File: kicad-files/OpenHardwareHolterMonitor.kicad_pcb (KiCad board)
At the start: 6 copper layers, 131 x 80 mm, 155 parts, among them CON1 Micro_SD_Card, J1 Conn_02x06_Odd_Even, J10 Conn_01x01, J11 Conn_01x01, J12 USB_OTG, J13 USB_C_Receptacle, J2 Conn_01x01, J3 Conn_01x01, J4 Conn_01x01, J5 Conn_01x01, J6 Conn_01x01, J7 Conn_01x01, J8 Conn_01x01, J9 Conn_01x01, P1 Custom_FTDI, Q1 S8050, Q10 Q_PMOS_DGS, Q2 S8050, Q3 Q_NMOS_DGS, Q4 Q_NMOS_DGS, Q5 Q_NMOS_DGS, Q6 Q_NMOS_DGS, Q7 Q_PMOS_DGS, Q8 Q_PMOS_DGS, Q9 Q_PMOS_DGS, SW1 SW_SPDT, U1 ESP-WROOM-32, U2 ADS1298, U3 MCP73833, U4 MCP73833, U5 TPS2113A, U6 LP5912, U7 REM_3-xxxxS, Y1 32768Hz

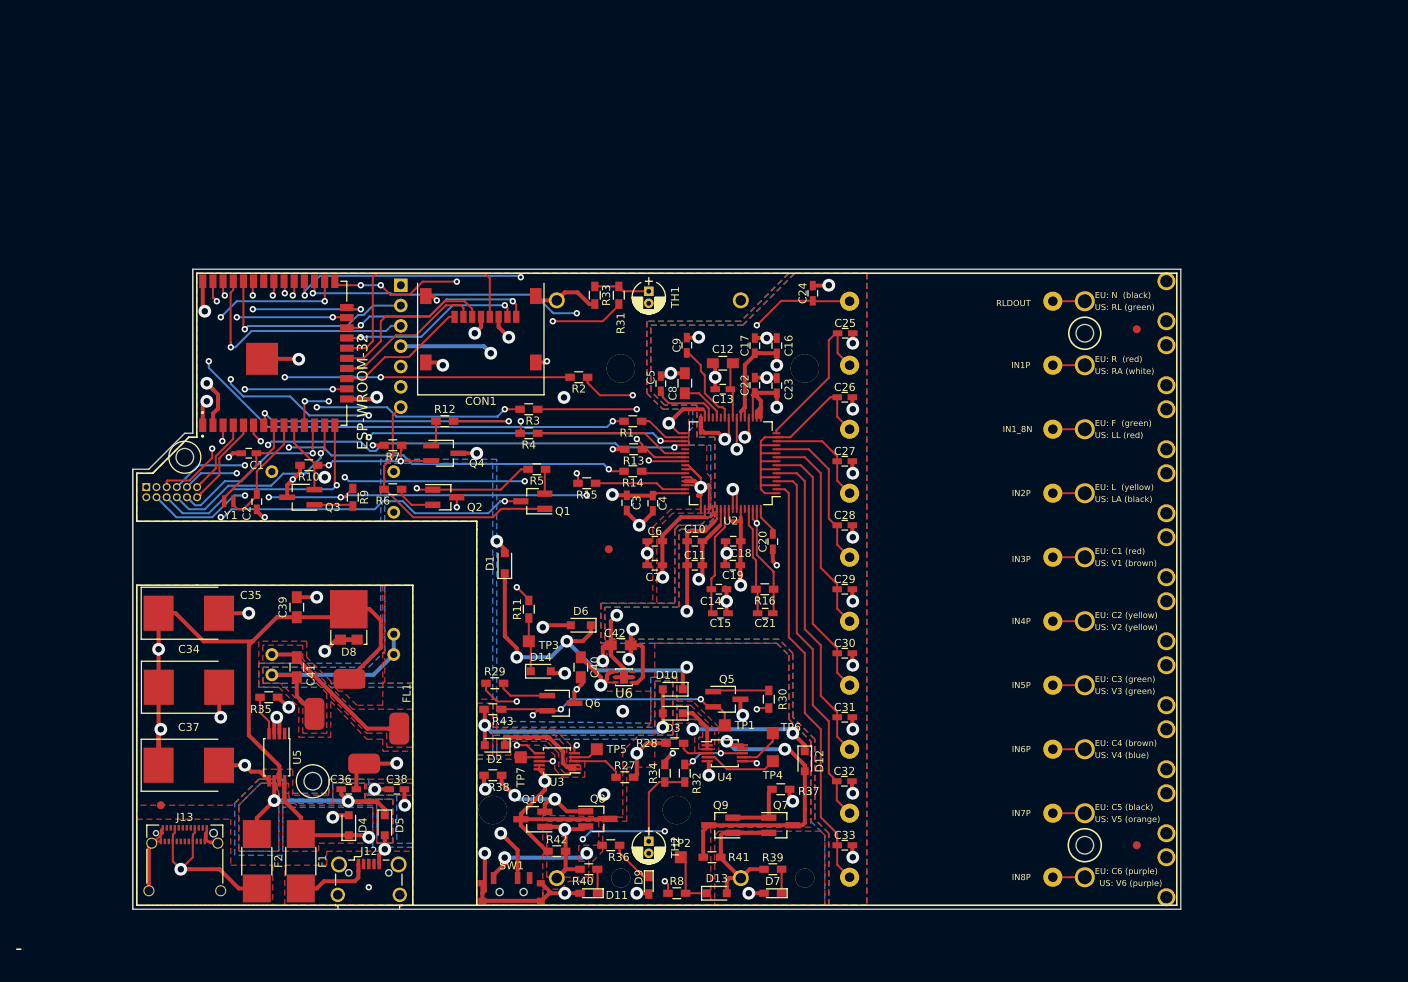
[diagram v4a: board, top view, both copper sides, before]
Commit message: Add logos and text to silkscreen layer
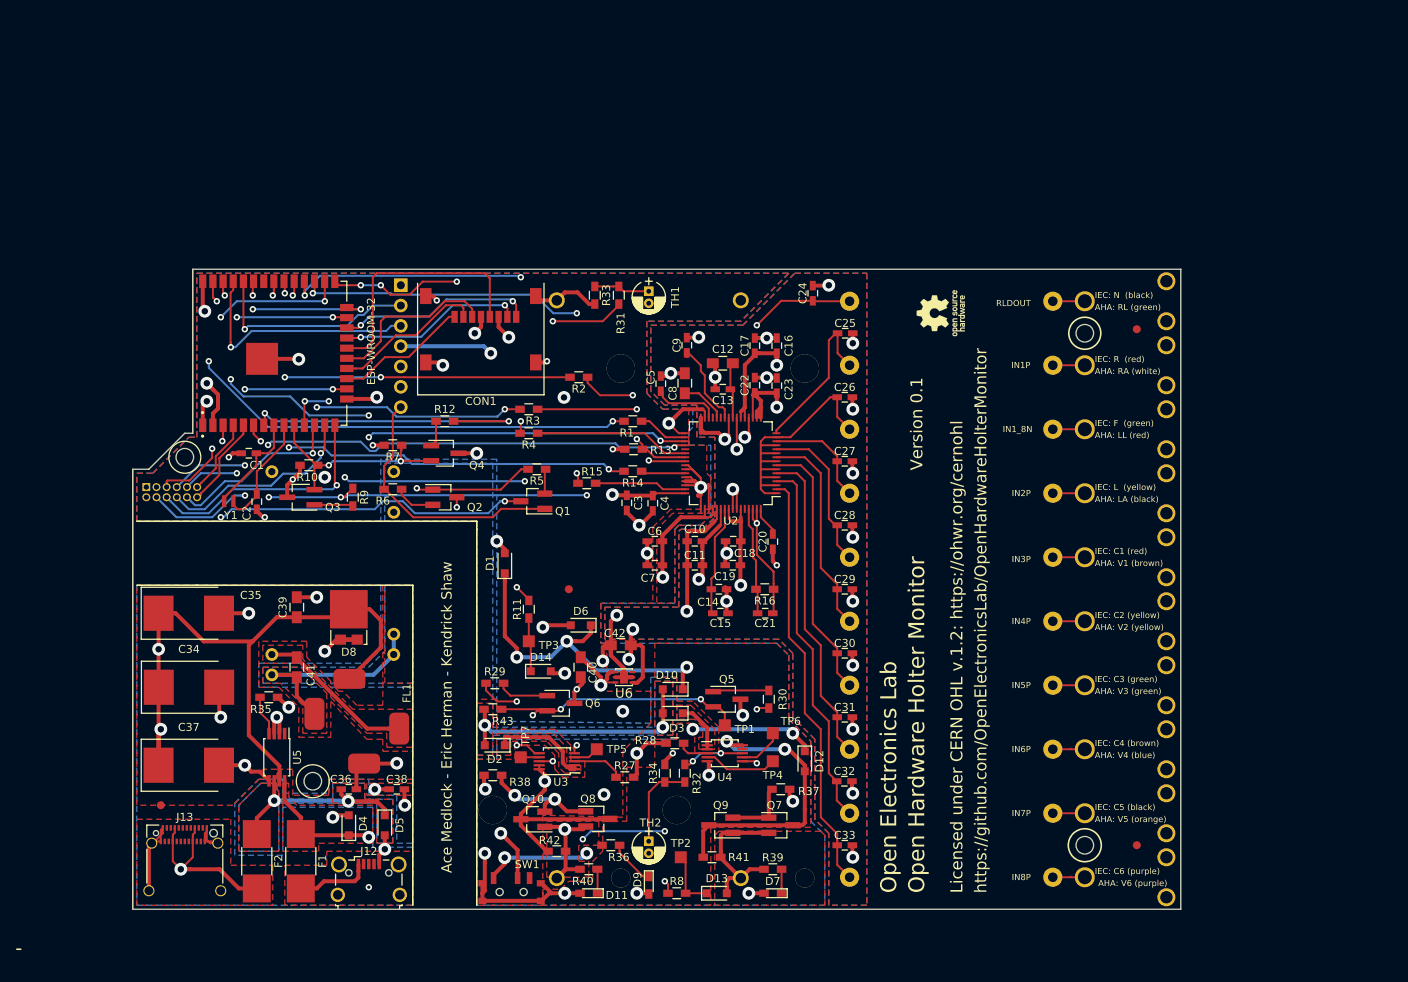
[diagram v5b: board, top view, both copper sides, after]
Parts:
- added REF**: OSHW-Logo_5.7x6mm_SilkScreen, Symbol:OSHW-Logo_5.7x6mm_SilkScreen, F.Cu at (240.0, 25.5)
- moved ? 7.07 mm to (193.5, 60.0)
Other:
- board text added: "AHA: LA (black)"
- board text added: "AHA: LL (red)"
- board text added: "AHA: RA (white)"
- board text added: "AHA: RL (green)"
- board text added: "AHA: V1 (brown)"
- board text added: "AHA: V2 (yellow)"
- board text added: "AHA: V3 (green)"
- board text added: "AHA: V4 (blue)"
- board text added: "AHA: V5 (orange)"
- board text added: "AHA: V6 (purple)"
- board text added: "Ace Medlock - Eric Herman - Kendrick Shaw"
- board text added: "IEC: C1 (red)"
- board text added: "IEC: C2 (yellow)"
- board text added: "IEC: C3 (green)"
- board text added: "IEC: C4 (brown)"
- board text added: "IEC: C5 (black)"
- board text added: "IEC: C6 (purple)"
- board text added: "IEC: F (green)"
- board text added: "IEC: L (yellow)"
- board text added: "IEC: N (black)"
- board text added: "IEC: R (red)"
- board text added: "Keepout zone for electrical isolation"
- board text added: "Licensed under CERN OHL v.1.2: https://ohwr.org/cernohl"
- board text added: "Open Electronics Lab"
- board text added: "Open Hardware Holter Monitor"
- board text added: "Version 0.1"
- board text added: "https://github.com/OpenElectronicsLab/OpenHardwareHolterMonitor"
- board text removed: "EU: C1 (red)"
- board text removed: "EU: C2 (yellow)"
- board text removed: "EU: C3 (green)"
- board text removed: "EU: C4 (brown)"
- board text removed: "EU: C5 (black)"
- board text removed: "EU: C6 (purple)"
- board text removed: "EU: F (green)"
- board text removed: "EU: L (yellow)"
- board text removed: "EU: N (black)"
- board text removed: "EU: R (red)"
- board text removed: "US: LA (black)"
- board text removed: "US: LL (red)"
- board text removed: "US: RA (white)"
- board text removed: "US: RL (green)"
- board text removed: "US: V1 (brown)"
- board text removed: "US: V2 (yellow)"
- board text removed: "US: V3 (green)"
- board text removed: "US: V4 (blue)"
- board text removed: "US: V5 (orange)"
- board text removed: "US: V6 (purple)"

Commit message: add gerber files
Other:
- rule pad_to_mask_clearance: 0.2 -> 0.0762
- rule solder_mask_min_width: 0.25 -> 0.2032
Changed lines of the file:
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@@
   (page A4)
   (layers
-    (0 F.Cu signal hide)
-    (1 In1.Cu.gnd power hide)
-    (2 In2.Cu.power power hide)
-    (3 In3.Cu.vert signal hide)
-    (4 In4.Cu.gnd power hide)
-    (31 B.Cu.horiz signal hide)
-    (32 B.Adhes user hide)
+    (0 F.Cu signal)
+    (1 In1.Cu.gnd power)
+    (2 In2.Cu.power power)
+    (3 In3.Cu.vert signal)
+    (4 In4.Cu.gnd power)
+    (31 B.Cu.horiz signal)
+    (32 B.Adhes user)
     (33 F.Adhes user)
-    (34 B.Paste user hide)
+    (34 B.Paste user)
     (35 F.Paste user)
-    (36 B.SilkS user hide)
+    (36 B.SilkS user)
     (37 F.SilkS user)
-    (38 B.Mask user hide)
+    (38 B.Mask user)
     (39 F.Mask user)
-    (40 Dwgs.User user hide)
+    (40 Dwgs.User user)
     (41 Cmts.User user)
     (42 Eco1.User user)
@@
     (44 Edge.Cuts user)
     (45 Margin user)
-    (46 B.CrtYd user hide)
+    (46 B.CrtYd user)
     (47 F.CrtYd user)
-    (48 B.Fab user hide)
-    (49 F.Fab user hide)
+    (48 B.Fab user)
+    (49 F.Fab user)
   )
   (setup
@@
     (pad_size 4 4)
     (pad_drill 0)
-    (pad_to_mask_clearance 0.2)
-    (solder_mask_min_width 0.25)
+    (pad_to_mask_clearance 0.0762)
+    (solder_mask_min_width 0.2032)
     (aux_axis_origin 0 0)
     (visible_elements FFFFFFFF)
@@
       (creategerberjobfile false)
       (excludeedgelayer true)
-      (linewidth 0.100000)
+      (linewidth 0.025400)
       (plotframeref false)
       (viasonmask false)
@@
       (outputformat 1)
       (mirror false)
-      (drillshape 1)
+      (drillshape 0)
       (scaleselection 1)
-      (outputdirectory ""))
+      (outputdirectory "ancillary-files/"))
   )
   (net 0 "")

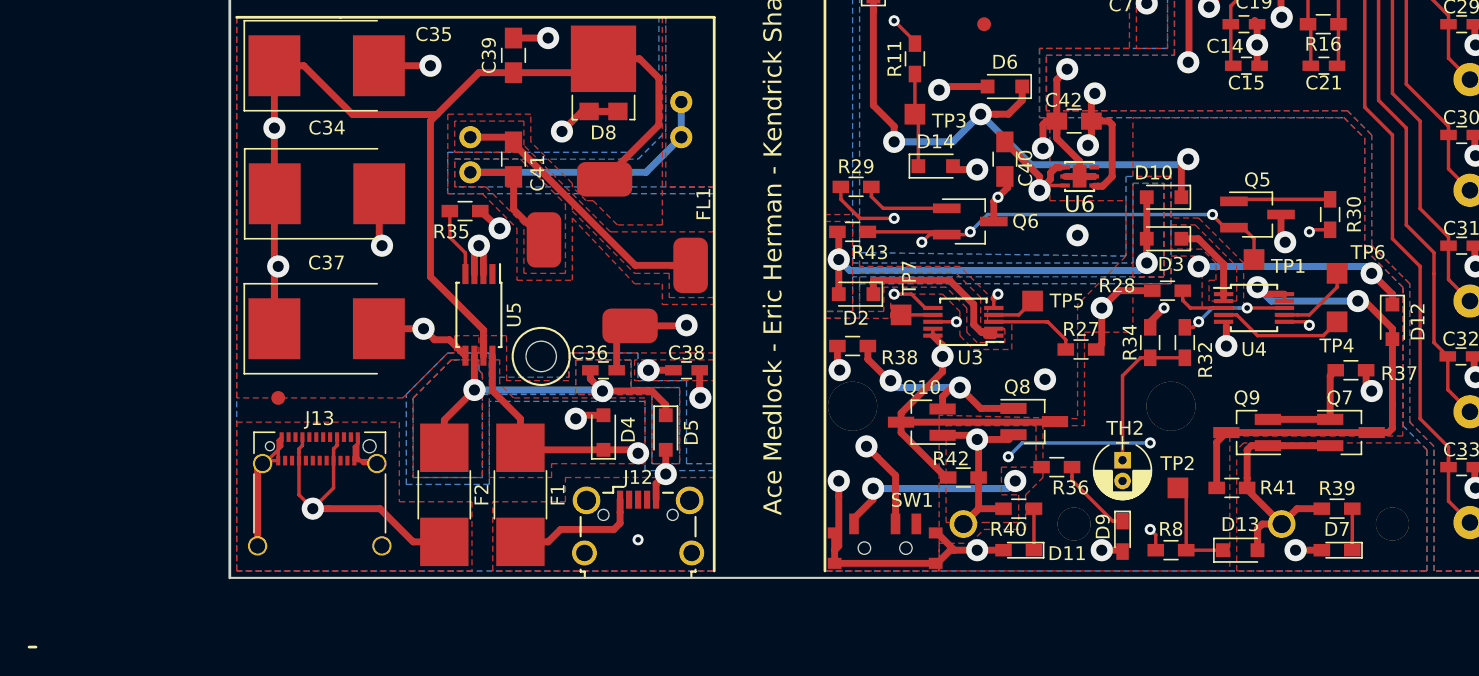
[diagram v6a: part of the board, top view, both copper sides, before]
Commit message: replace switch and rework pcb
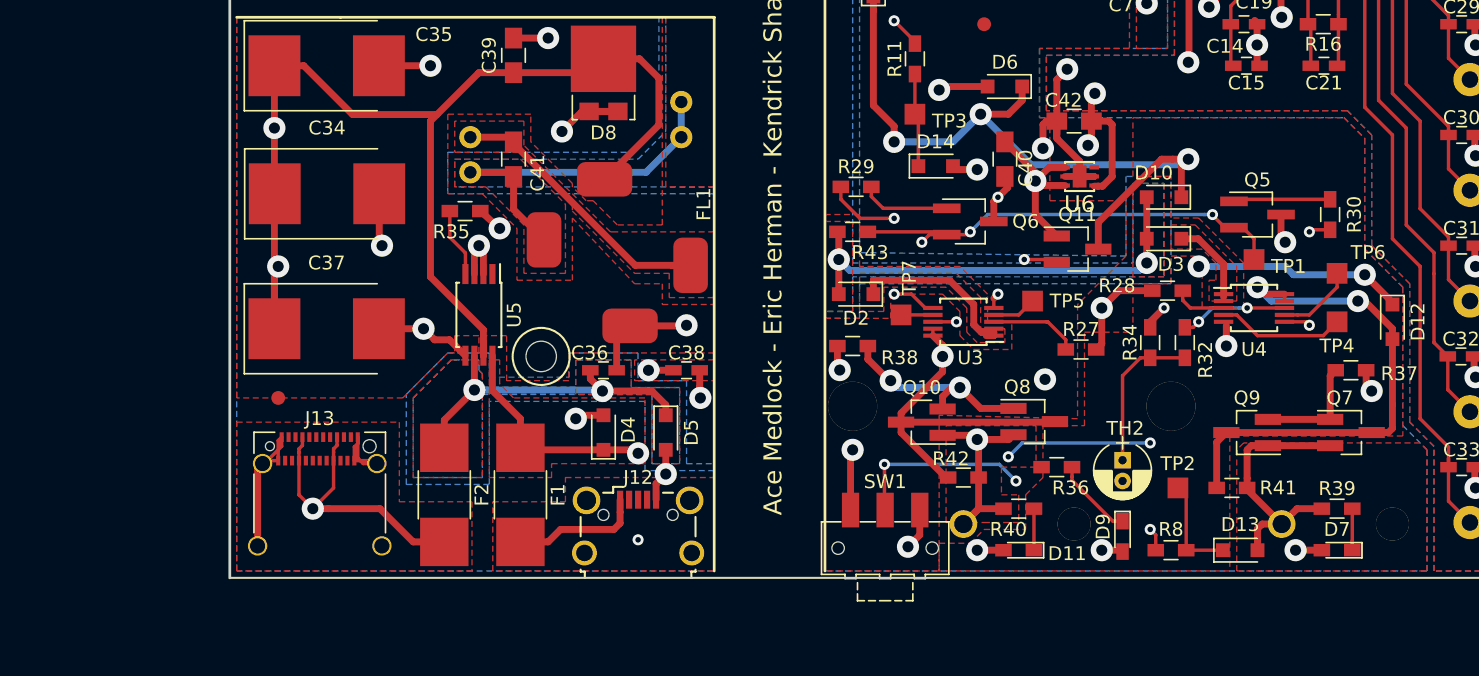
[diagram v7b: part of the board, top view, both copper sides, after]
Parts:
- added Q11: Q_PMOS_DGS, TO_SOT_Packages_SMD:SOT-23_Handsoldering, F.Cu at (200.2, 76.2)
- C36, C38: value 0.1uF -> 100nF
- SW1: footprint Alps:ALPS_SSSS810701 -> Buttons_Switches_SMD:SW_SPDT_CK-JS102011SAQN
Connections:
- C40 pad 1: Net-(C40-Pad1) -> /power/REGULATOR_IN
- D1 pad 1: /power/REGULATOR_IN -> /power/SWITCH_IN
- D10 pad 1: /power/REGULATOR_IN -> /power/SWITCH_IN
- D12 pad 1: /power/REGULATOR_IN -> /power/SWITCH_IN
- D6 pad 1: /power/REGULATOR_IN -> /power/SWITCH_IN
- SW1 pad 1: Net-(C40-Pad1) -> /power/SWITCH_IN
- SW1 pad 2: /power/REGULATOR_IN -> Net-(Q11-Pad2)
- SW1 pad 3: Net-(SW1-Pad3) -> GND
- U6 pad 4: Net-(C40-Pad1) -> /power/REGULATOR_IN
- U6 pad 6: Net-(C40-Pad1) -> /power/REGULATOR_IN
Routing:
- net /power/SWITCH_IN: track 0.00 -> 104.9 mm, vias 0 -> 6
- net /power/REGULATOR_IN: track 96.3 -> 13.2 mm, vias 6 -> 1
- net Net-(C40-Pad1): track 45.1 -> 0.00 mm, vias 3 -> 0
- net Net-(Q11-Pad2): track 0.00 -> 32.0 mm, vias 0 -> 3
- net GND: track 222.6 -> 194.3 mm, vias 56 -> 55

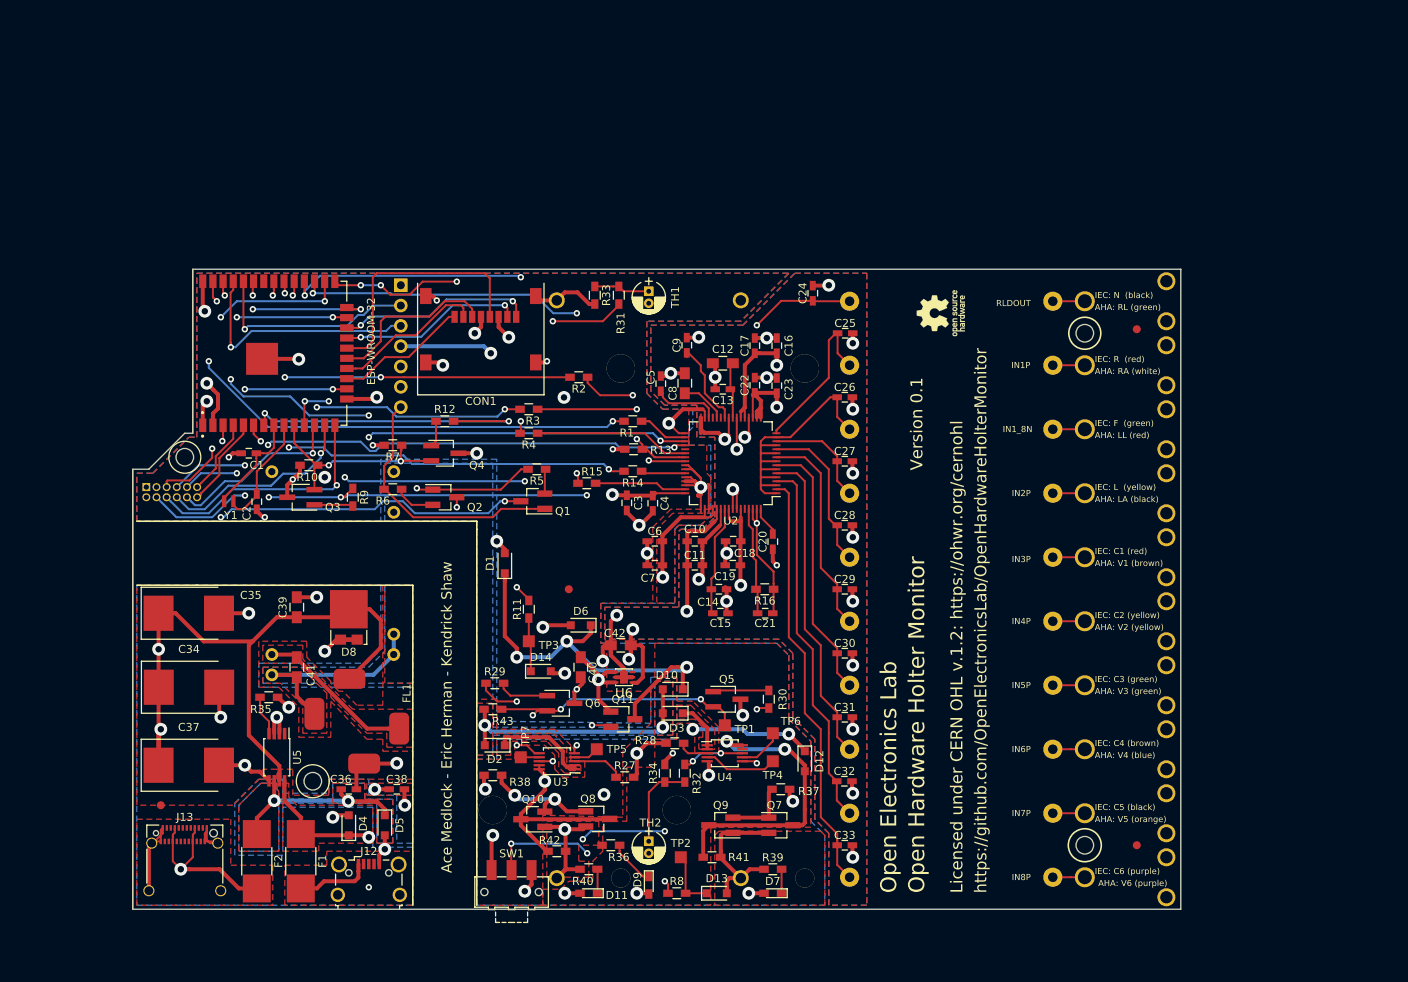
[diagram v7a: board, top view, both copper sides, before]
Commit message: flipped alternating resistors to increase clearance between
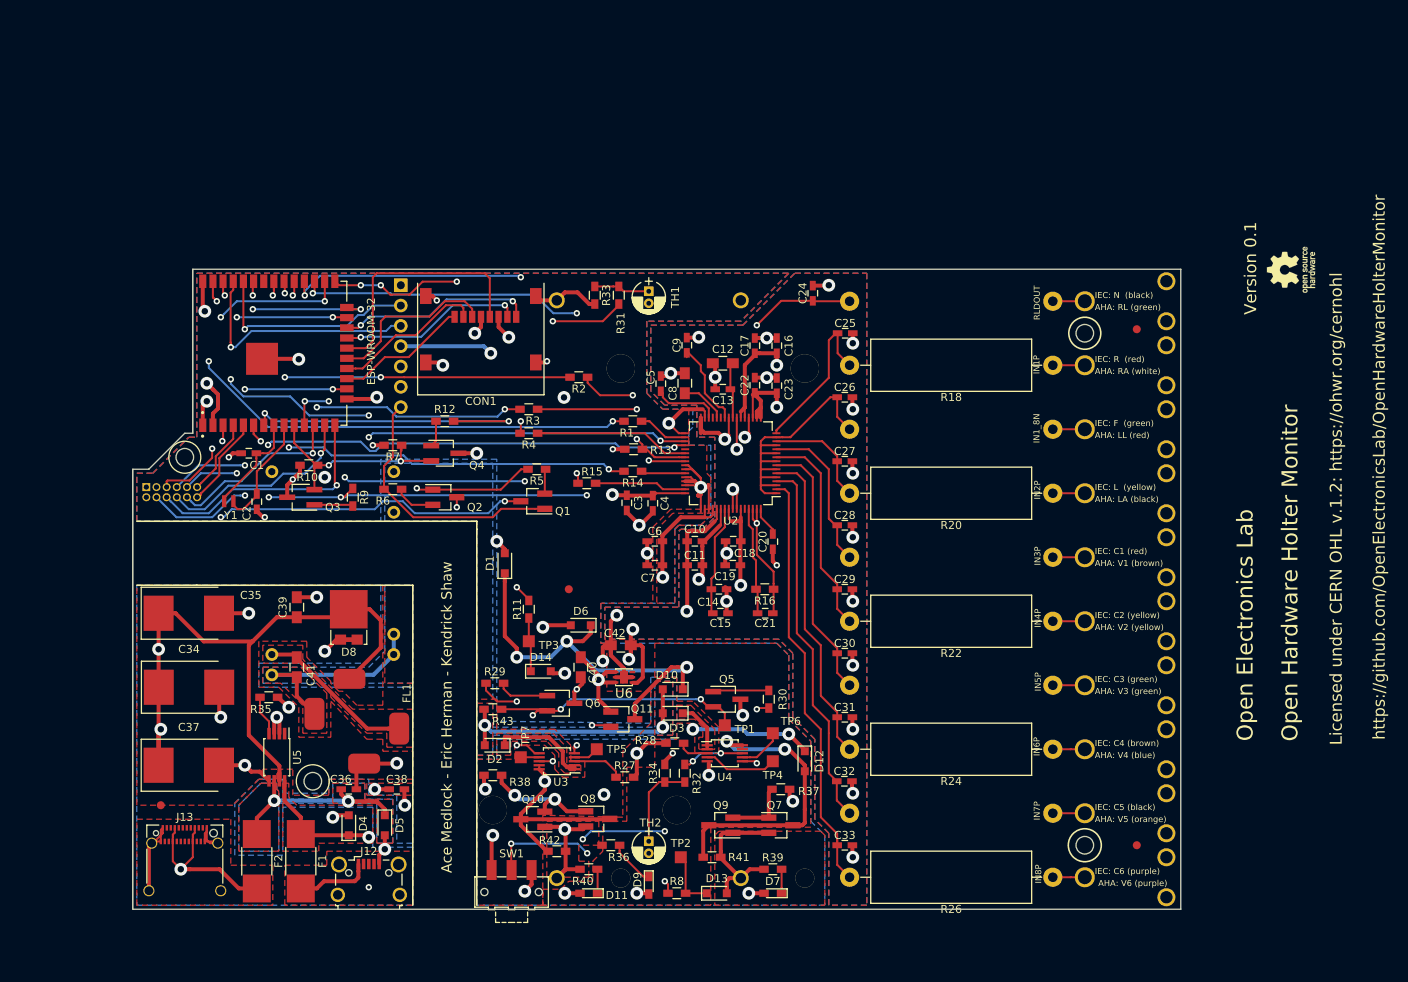
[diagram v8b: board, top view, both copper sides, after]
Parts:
- R18, R20, R22, R24, R26: moved to F.Cu
- moved REF** 44.1 mm to (283.8, 20.1)
